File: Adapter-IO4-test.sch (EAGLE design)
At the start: 19 parts, among them CON1 CONNECTOR-IO4INV, Q1 P-FET, Q2 P-FET, Q3 P-FET, Q4 P-FET, SW1 SPST-MOM, SW2 SPST-MOM, SW3 SPST-MOM, SW4 SPST-MOM

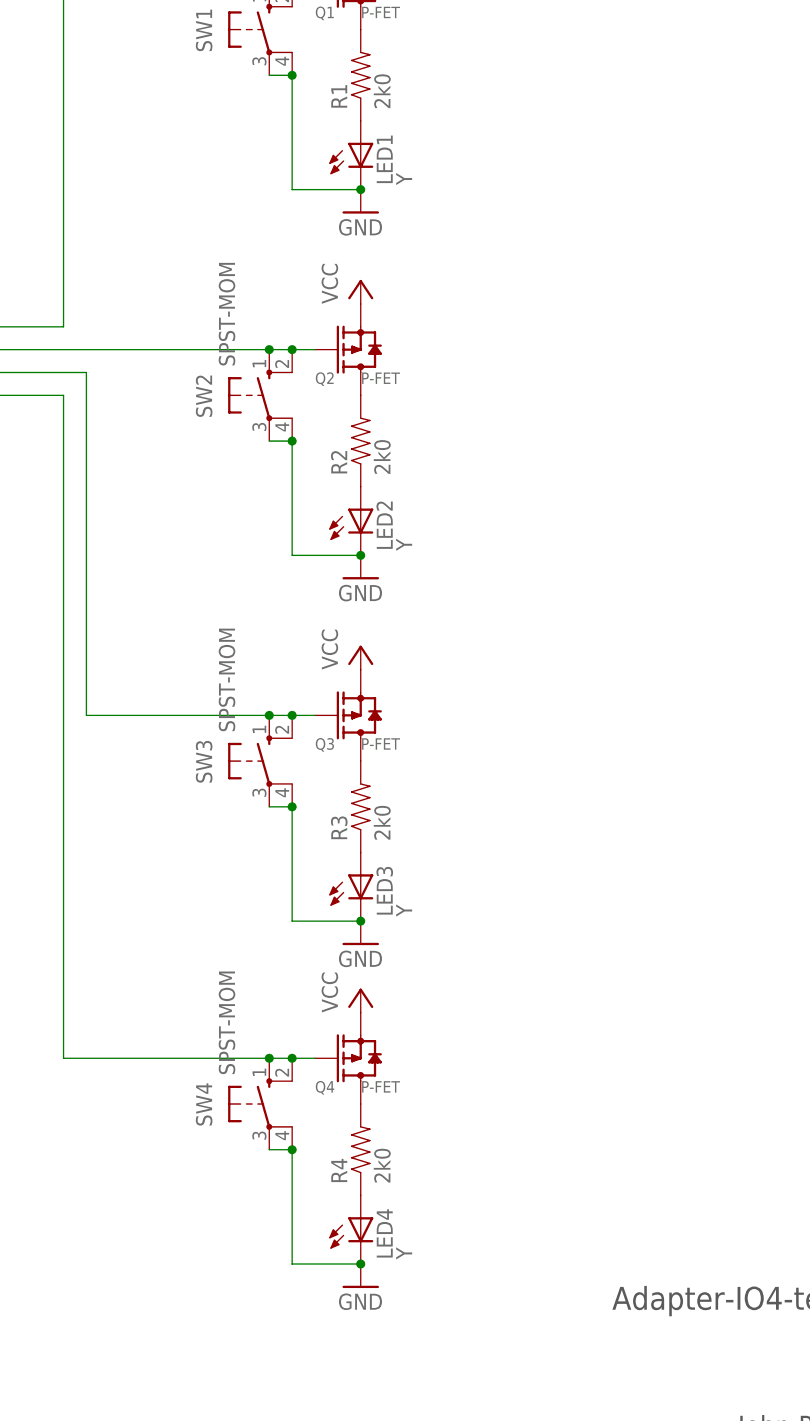
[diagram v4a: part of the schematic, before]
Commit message: added value G to LEDs
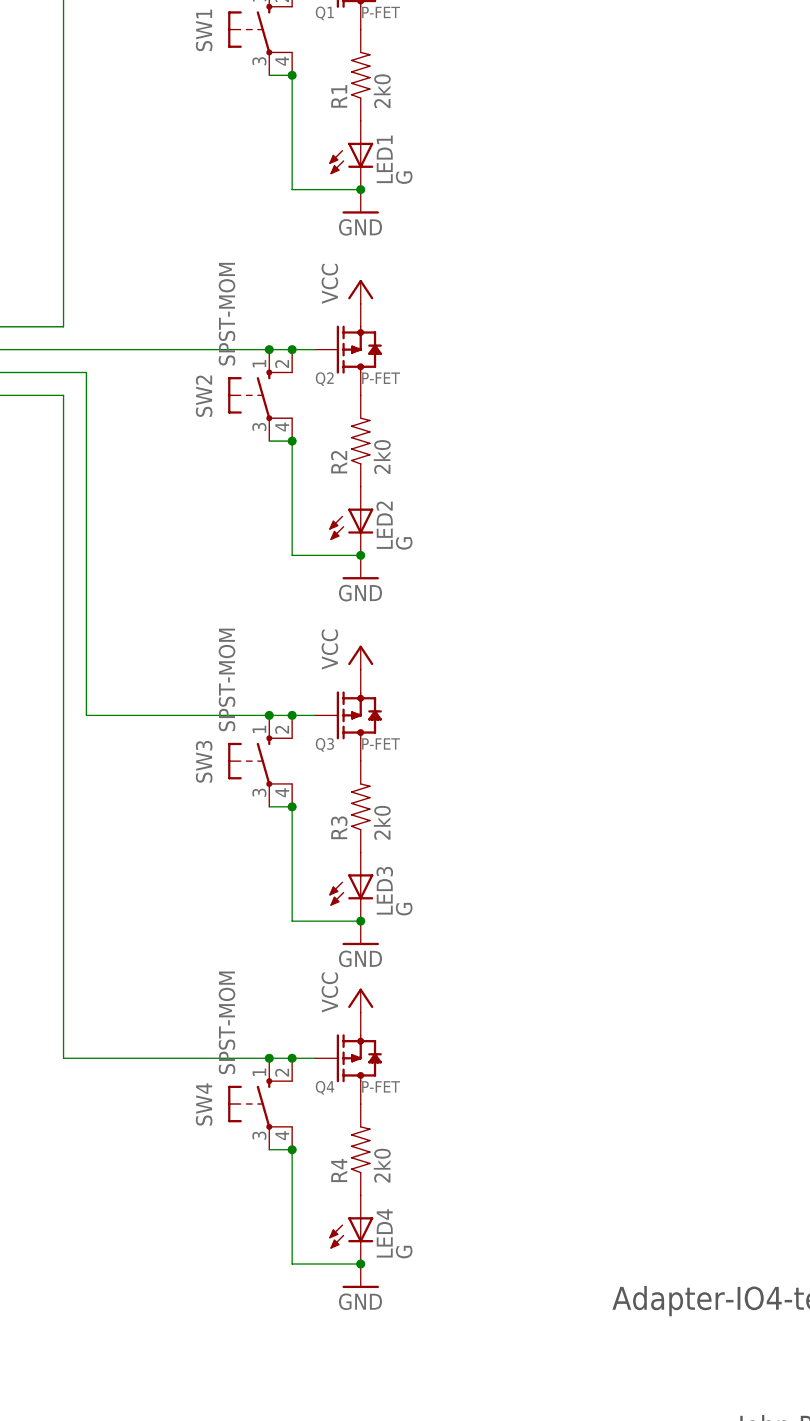
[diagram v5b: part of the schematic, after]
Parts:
- LED1, LED2, LED3, LED4: value Y -> G
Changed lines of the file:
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@@
 <part name="P+1" library="SPCoast" deviceset="VCC" device=""/>
 <part name="GND1" library="SPCoast" deviceset="GND" device=""/>
-<part name="LED1" library="SPCoast" deviceset="LED*" device="0805-LED" value="Y"/>
-<part name="LED2" library="SPCoast" deviceset="LED*" device="0805-LED" value="Y"/>
-<part name="LED3" library="SPCoast" deviceset="LED*" device="0805-LED" value="Y"/>
-<part name="LED4" library="SPCoast" deviceset="LED*" device="0805-LED" value="Y"/>
+<part name="LED1" library="SPCoast" deviceset="LED*" device="0805-LED" value="G"/>
+<part name="LED2" library="SPCoast" deviceset="LED*" device="0805-LED" value="G"/>
+<part name="LED3" library="SPCoast" deviceset="LED*" device="0805-LED" value="G"/>
+<part name="LED4" library="SPCoast" deviceset="LED*" device="0805-LED" value="G"/>
 <part name="R1" library="SPCoast" deviceset="R*" device="0805-RES" value="2k0"/>
 <part name="R2" library="SPCoast" deviceset="R*" device="0805-RES" value="2k0"/>

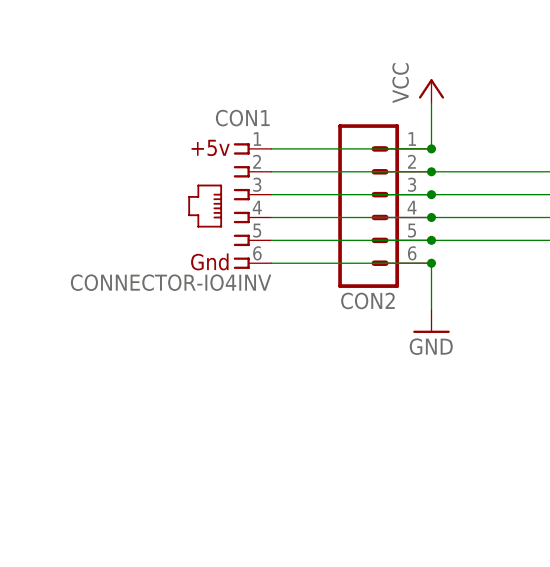
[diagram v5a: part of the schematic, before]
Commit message: fixed SPCoast lbr part orientation
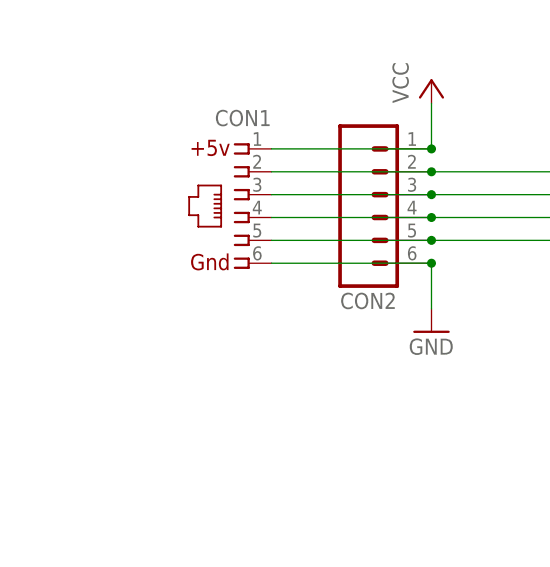
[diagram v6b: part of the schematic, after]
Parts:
- CON1: value CONNECTOR-IO4INV -> (none)

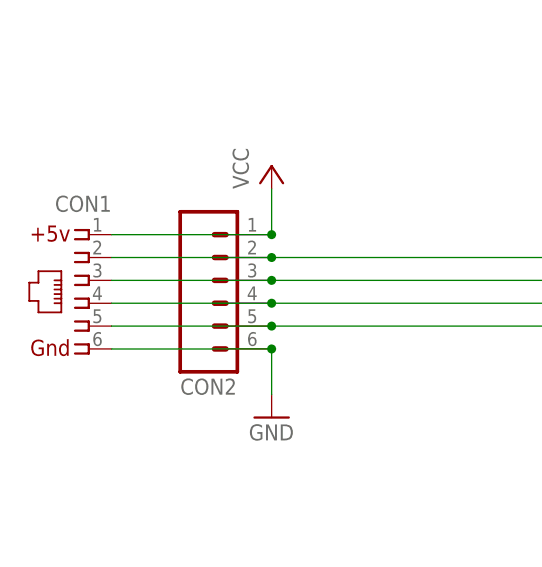
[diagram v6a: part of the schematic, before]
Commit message: added values for connectors
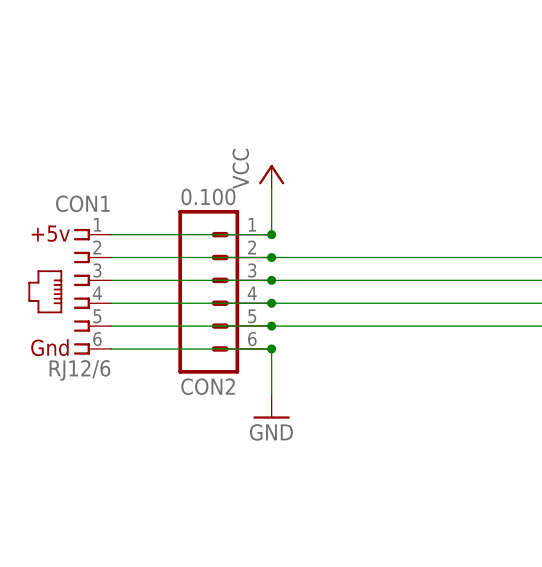
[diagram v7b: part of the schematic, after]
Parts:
- CON1: value (none) -> RJ12/6
- CON2: value (none) -> 0.100
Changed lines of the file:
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@@
 <parts>
 <part name="FRAME1" library="SPCoast" deviceset="DOC-FRAME-LETTER" device=""/>
-<part name="CON1" library="SPCoast" deviceset="CONNECTOR-IO4" device="INV"/>
-<part name="CON2" library="SPCoast" deviceset="CONNECTOR-M06" device="LOCK"/>
+<part name="CON1" library="SPCoast" deviceset="CONNECTOR-IO4" device="INV" value="RJ12/6"/>
+<part name="CON2" library="SPCoast" deviceset="CONNECTOR-M06" device="LOCK" value="0.100"/>
 <part name="Q1" library="SPCoast" deviceset="MOSFET-P" device="" value="P-FET"/>
 <part name="Q2" library="SPCoast" deviceset="MOSFET-P" device="" value="P-FET"/>

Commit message: normalized values
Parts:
- LED1, LED2, LED3, LED4: device SPCoast:LED0805-LED -> SPCoast:LED0603-LED
- R1, R2, R3, R4: device SPCoast:R0805-RES -> SPCoast:R0603-RES
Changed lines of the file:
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@@
 <grid distance="100" unitdist="mil" unit="mil" style="dots" multiple="1" display="yes" altdistance="50" altunitdist="mil" altunit="mil"/>
 <layers>
-<layer number="1" name="Top" color="4" fill="1" visible="no" active="no"/>
-<layer number="2" name="Route2" color="1" fill="3" visible="no" active="no"/>
-<layer number="3" name="Route3" color="4" fill="3" visible="no" active="no"/>
-<layer number="14" name="Route14" color="1" fill="6" visible="no" active="no"/>
-<layer number="15" name="Route15" color="4" fill="6" visible="no" active="no"/>
-<layer number="16" name="Bottom" color="2" fill="1" visible="no" active="no"/>
-<layer number="17" name="Pads" color="23" fill="1" visible="no" active="no"/>
-<layer number="18" name="Vias" color="29" fill="1" visible="no" active="no"/>
-<layer number="19" name="Unrouted" color="6" fill="1" visible="no" active="no"/>
-<layer number="20" name="Dimension" color="15" fill="1" visible="no" active="no"/>
-<layer number="21" name="tPlace" color="19" fill="1" visible="no" active="no"/>
-<layer number="22" name="bPlace" color="17" fill="1" visible="no" active="no"/>
-<layer number="23" name="tOrigins" color="30" fill="1" visible="no" active="no"/>
-<layer number="24" name="bOrigins" color="15" fill="1" visible="no" active="no"/>
-<layer number="25" name="tNames" color="63" fill="1" visible="no" active="no"/>
-<layer number="26" name="bNames" color="34" fill="1" visible="no" active="no"/>
-<layer number="27" name="tValues" color="56" fill="1" visible="no" active="no"/>
-<layer number="28" name="bValues" color="7" fill="1" visible="no" active="no"/>
+<layer number="1" name="Top" color="4" fill="1" visible="yes" active="no"/>
+<layer number="2" name="Route2" color="1" fill="3" visible="yes" active="no"/>
+<layer number="3" name="Route3" color="4" fill="3" visible="yes" active="no"/>
+<layer number="14" name="Route14" color="1" fill="6" visible="yes" active="no"/>
+<layer number="15" name="Route15" color="4" fill="6" visible="yes" active="no"/>
+<layer number="16" name="Bottom" color="2" fill="1" visible="yes" active="no"/>
+<layer number="17" name="Pads" color="23" fill="1" visible="yes" active="no"/>
+<layer number="18" name="Vias" color="29" fill="1" visible="yes" active="no"/>
+<layer number="19" name="Unrouted" color="6" fill="1" visible="yes" active="no"/>
+<layer number="20" name="Dimension" color="15" fill="1" visible="yes" active="no"/>
+<layer number="21" name="tPlace" color="19" fill="1" visible="yes" active="no"/>
+<layer number="22" name="bPlace" color="17" fill="1" visible="yes" active="no"/>
+<layer number="23" name="tOrigins" color="30" fill="1" visible="yes" active="no"/>
+<layer number="24" name="bOrigins" color="15" fill="1" visible="yes" active="no"/>
+<layer number="25" name="tNames" color="63" fill="1" visible="yes" active="no"/>
+<layer number="26" name="bNames" color="34" fill="1" visible="yes" active="no"/>
+<layer number="27" name="tValues" color="56" fill="1" visible="yes" active="no"/>
+<layer number="28" name="bValues" color="7" fill="1" visible="yes" active="no"/>
 <layer number="29" name="tStop" color="7" fill="3" visible="no" active="no"/>
 <layer number="30" name="bStop" color="7" fill="6" visible="no" active="no"/>
@@
 <layer number="35" name="tGlue" color="7" fill="4" visible="no" active="no"/>
 <layer number="36" name="bGlue" color="7" fill="5" visible="no" active="no"/>
-<layer number="37" name="tTest" color="7" fill="1" visible="no" active="no"/>
-<layer number="38" name="bTest" color="7" fill="1" visible="no" active="no"/>
+<layer number="37" name="tTest" color="7" fill="1" visible="yes" active="no"/>
+<layer number="38" name="bTest" color="7" fill="1" visible="yes" active="no"/>
 <layer number="39" name="tKeepout" color="4" fill="11" visible="no" active="no"/>
 <layer number="40" name="bKeepout" color="3" fill="11" visible="no" active="no"/>
@@
 <layer number="44" name="Drills" color="16" fill="1" visible="no" active="no"/>
 <layer number="45" name="Holes" color="35" fill="1" visible="no" active="no"/>
-<layer number="46" name="Milling" color="35" fill="1" visible="no" active="no"/>
-<layer number="47" name="Measures" color="21" fill="1" visible="no" active="no"/>
-<layer number="48" name="Document" color="47" fill="1" visible="no" active="no"/>
-<layer number="49" name="Reference" color="48" fill="1" visible="no" active="no"/>
-<layer number="50" name="dxf" color="7" fill="1" visible="no" active="no"/>
-<layer number="51" name="tDocu" color="24" fill="1" visible="no" active="no"/>
-<layer number="52" name="bDocu" color="7" fill="1" visible="no" active="no"/>
-<layer number="53" name="tGND_GNDA" color="7" fill="9" visible="no" active="no"/>
-<layer number="54" name="bGND_GNDA" color="1" fill="9" visible="no" active="no"/>
-<layer number="56" name="wert" color="7" fill="1" visible="no" active="no"/>
-<layer number="57" name="tCAD" color="7" fill="1" visible="no" active="no"/>
-<layer number="59" name="tCarbon" color="7" fill="1" visible="no" active="no"/>
-<layer number="60" name="bCarbon" color="7" fill="1" visible="no" active="no"/>
+<layer number="46" name="Milling" color="35" fill="1" visible="yes" active="no"/>
+<layer number="47" name="Measures" color="21" fill="1" visible="yes" active="no"/>
+<layer number="48" name="Document" color="47" fill="1" visible="yes" active="no"/>
+<layer number="49" name="Reference" color="48" fill="1" visible="yes" active="no"/>
+<layer number="50" name="dxf" color="7" fill="1" visible="yes" active="no"/>
+<layer number="51" name="tDocu" color="24" fill="1" visible="yes" active="no"/>
+<layer number="52" name="bDocu" color="7" fill="1" visible="yes" active="no"/>
+<layer number="53" name="tGND_GNDA" color="7" fill="9" visible="yes" active="no"/>
+<layer number="54" name="bGND_GNDA" color="1" fill="9" visible="yes" active="no"/>
+<layer number="56" name="wert" color="7" fill="1" visible="yes" active="no"/>
+<layer number="57" name="tCAD" color="7" fill="1" visible="yes" active="no"/>
+<layer number="59" name="tCarbon" color="7" fill="1" visible="yes" active="no"/>
+<layer number="60" name="bCarbon" color="7" fill="1" visible="yes" active="no"/>
 <layer number="90" name="Modules" color="5" fill="1" visible="yes" active="yes"/>
 <layer number="91" name="Nets" color="2" fill="1" visible="yes" active="yes"/>
@@
 <part name="P+1" library="SPCoast" deviceset="VCC" device=""/>
 <part name="GND1" library="SPCoast" deviceset="GND" device=""/>
-<part name="LED1" library="SPCoast" deviceset="LED*" device="0805-LED" value="G"/>
-<part name="LED2" library="SPCoast" deviceset="LED*" device="0805-LED" value="G"/>
-<part name="LED3" library="SPCoast" deviceset="LED*" device="0805-LED" value="G"/>
-<part name="LED4" library="SPCoast" deviceset="LED*" device="0805-LED" value="G"/>
-<part name="R1" library="SPCoast" deviceset="R*" device="0805-RES" value="2k0"/>
-<part name="R2" library="SPCoast" deviceset="R*" device="0805-RES" value="2k0"/>
-<part name="R3" library="SPCoast" deviceset="R*" device="0805-RES" value="2k0"/>
-<part name="R4" library="SPCoast" deviceset="R*" device="0805-RES" value="2k0"/>
+<part name="LED1" library="SPCoast" deviceset="LED*" device="0603-LED" value="G"/>
+<part name="LED2" library="SPCoast" deviceset="LED*" device="0603-LED" value="G"/>
+<part name="LED3" library="SPCoast" deviceset="LED*" device="0603-LED" value="G"/>
+<part name="LED4" library="SPCoast" deviceset="LED*" device="0603-LED" value="G"/>
+<part name="R1" library="SPCoast" deviceset="R*" device="0603-RES" value="2k0"/>
+<part name="R2" library="SPCoast" deviceset="R*" device="0603-RES" value="2k0"/>
+<part name="R3" library="SPCoast" deviceset="R*" device="0603-RES" value="2k0"/>
+<part name="R4" library="SPCoast" deviceset="R*" device="0603-RES" value="2k0"/>
 <part name="P+2" library="SPCoast" deviceset="VCC" device=""/>
 <part name="GND2" library="SPCoast" deviceset="GND" device=""/>
